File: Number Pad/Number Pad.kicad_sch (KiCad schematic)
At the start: 40 parts

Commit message: Added connectors, labeled keys
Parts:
- added J?: Conn_01x04_Male, symbol Connector:Conn_01x04_Male
- added J?: Conn_01x04_Female, symbol Connector:Conn_01x04_Female
- gave numbers to parts that had none: 18

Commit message: Added footprint libraries
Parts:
- removed J?: Conn_01x04_Male, symbol Connector:Conn_01x04_Male
- removed J?: Conn_01x04_Female, symbol Connector:Conn_01x04_Female
- added J1: Conn_01x05_Female, Connector_JST:JST_PH_S6B-PH-K_1x06_P2.00mm_Horizontal, symbol Connector:Conn_01x05_Female
- added J2: Conn_01x05_Male, Connector_JST:JST_PH_S5B-PH-K_1x05_P2.00mm_Horizontal, symbol Connector:Conn_01x05_Male
- added R1, R2: 100, Resistor_SMD:R_0805_2012Metric, symbol Device:R_Small
- D1, D10, D11, D12, D13, D14, D15, D16, D17, D18, D19, D2, D20, D3, D4, D5, D6, D7, D8, D9: renamed from D?; footprint (none) -> Diode_SMD:D_SOD-123
- renumbered MX_* to MX_*1, MX_+ to MX_+1, MX_- to MX_-1, MX_. to MX_.1, MX_/ to MX_/1, MX_0 to MX_0k1, MX_0 to MX_0k2, MX_Bksp to MX_Bksp1, MX_Enter to MX_Enter1, MX_Enter to MX_Enter2, MX_Num_Lock to MX_Num_Lock1
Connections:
- new net: J2.3 (Pin_3), R2.1
- new net: J1.3 (Pin_3), R1.2
- new net GND: J1.5 (Pin_5), J2.5 (Pin_5)
- new net IN: R2.2
- new net OUT: R1.1
- new net VCC: J1.1 (Pin_1), J2.1 (Pin_1)

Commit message: Assigned footprints
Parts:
- MX_*1, MX_+1, MX_-1, MX_.1, MX_/1, MX_0k1, MX_0k2, MX_1, MX_2, MX_3, MX_4, MX_5, MX_6, MX_7, MX_8, MX_9, MX_Bksp1, MX_Enter1, MX_Enter2, MX_Num_Lock1: footprint (none) -> MX_Alps_Hybrid:MX-1U-NoLED
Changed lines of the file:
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@@
       (effects (font (size 0.508 0.508)))
     )
-    (property "Footprint" "" (id 2) (at 104.775 116.205 0)
+    (property "Footprint" "MX_Alps_Hybrid:MX-1U-NoLED" (id 2) (at 104.775 116.205 0)
       (effects (font (size 1.524 1.524)) hide)
     )
@@
       (effects (font (size 0.508 0.508)))
     )
-    (property "Footprint" "" (id 2) (at 90.805 133.985 0)
+    (property "Footprint" "MX_Alps_Hybrid:MX-1U-NoLED" (id 2) (at 90.805 133.985 0)
       (effects (font (size 1.524 1.524)) hide)
     )
@@
       (effects (font (size 0.508 0.508)))
     )
-    (property "Footprint" "" (id 2) (at 104.775 80.645 0)
+    (property "Footprint" "MX_Alps_Hybrid:MX-1U-NoLED" (id 2) (at 104.775 80.645 0)
       (effects (font (size 1.524 1.524)) hide)
     )
@@
       (effects (font (size 0.508 0.508)))
     )
-    (property "Footprint" "" (id 2) (at 104.775 98.425 0)
+    (property "Footprint" "MX_Alps_Hybrid:MX-1U-NoLED" (id 2) (at 104.775 98.425 0)
       (effects (font (size 1.524 1.524)) hide)
     )
@@
       (effects (font (size 0.508 0.508)))
     )
-    (property "Footprint" "" (id 2) (at 120.015 133.985 0)
+    (property "Footprint" "MX_Alps_Hybrid:MX-1U-NoLED" (id 2) (at 120.015 133.985 0)
       (effects (font (size 1.524 1.524)) hide)
     )
@@
       (effects (font (size 0.508 0.508)))
     )
-    (property "Footprint" "" (id 2) (at 90.805 116.205 0)
+    (property "Footprint" "MX_Alps_Hybrid:MX-1U-NoLED" (id 2) (at 90.805 116.205 0)
       (effects (font (size 1.524 1.524)) hide)
     )
@@
       (effects (font (size 0.508 0.508)))
     )
-    (property "Footprint" "" (id 2) (at 76.835 116.205 0)
+    (property "Footprint" "MX_Alps_Hybrid:MX-1U-NoLED" (id 2) (at 76.835 116.205 0)
       (effects (font (size 1.524 1.524)) hide)
     )
@@
       (effects (font (size 0.508 0.508)))
     )
-    (property "Footprint" "" (id 2) (at 76.835 133.985 0)
+    (property "Footprint" "MX_Alps_Hybrid:MX-1U-NoLED" (id 2) (at 76.835 133.985 0)
       (effects (font (size 1.524 1.524)) hide)
     )
@@
       (effects (font (size 0.508 0.508)))
     )
-    (property "Footprint" "" (id 2) (at 76.835 62.865 0)
+    (property "Footprint" "MX_Alps_Hybrid:MX-1U-NoLED" (id 2) (at 76.835 62.865 0)
       (effects (font (size 1.524 1.524)) hide)
     )
@@
       (effects (font (size 0.508 0.508)))
     )
-    (property "Footprint" "" (id 2) (at 120.015 80.645 0)
+    (property "Footprint" "MX_Alps_Hybrid:MX-1U-NoLED" (id 2) (at 120.015 80.645 0)
       (effects (font (size 1.524 1.524)) hide)
     )
@@
       (effects (font (size 0.508 0.508)))
     )
-    (property "Footprint" "" (id 2) (at 120.015 116.205 0)
+    (property "Footprint" "MX_Alps_Hybrid:MX-1U-NoLED" (id 2) (at 120.015 116.205 0)
       (effects (font (size 1.524 1.524)) hide)
     )
@@
       (effects (font (size 0.508 0.508)))
     )
-    (property "Footprint" "" (id 2) (at 120.015 98.425 0)
+    (property "Footprint" "MX_Alps_Hybrid:MX-1U-NoLED" (id 2) (at 120.015 98.425 0)
       (effects (font (size 1.524 1.524)) hide)
     )
@@
       (effects (font (size 0.508 0.508)))
     )
-    (property "Footprint" "" (id 2) (at 104.775 133.985 0)
+    (property "Footprint" "MX_Alps_Hybrid:MX-1U-NoLED" (id 2) (at 104.775 133.985 0)
       (effects (font (size 1.524 1.524)) hide)
     )
@@
       (effects (font (size 0.508 0.508)))
     )
-    (property "Footprint" "" (id 2) (at 90.805 62.865 0)
+    (property "Footprint" "MX_Alps_Hybrid:MX-1U-NoLED" (id 2) (at 90.805 62.865 0)
       (effects (font (size 1.524 1.524)) hide)
     )
@@
       (effects (font (size 0.508 0.508)))
     )
-    (property "Footprint" "" (id 2) (at 90.805 80.645 0)
+    (property "Footprint" "MX_Alps_Hybrid:MX-1U-NoLED" (id 2) (at 90.805 80.645 0)
       (effects (font (size 1.524 1.524)) hide)
     )
@@
       (effects (font (size 0.508 0.508)))
     )
-    (property "Footprint" "" (id 2) (at 76.835 98.425 0)
+    (property "Footprint" "MX_Alps_Hybrid:MX-1U-NoLED" (id 2) (at 76.835 98.425 0)
       (effects (font (size 1.524 1.524)) hide)
     )
@@
       (effects (font (size 0.508 0.508)))
     )
-    (property "Footprint" "" (id 2) (at 76.835 80.645 0)
+    (property "Footprint" "MX_Alps_Hybrid:MX-1U-NoLED" (id 2) (at 76.835 80.645 0)
       (effects (font (size 1.524 1.524)) hide)
     )
@@
       (effects (font (size 0.508 0.508)))
     )
-    (property "Footprint" "" (id 2) (at 104.775 62.865 0)
+    (property "Footprint" "MX_Alps_Hybrid:MX-1U-NoLED" (id 2) (at 104.775 62.865 0)
       (effects (font (size 1.524 1.524)) hide)
     )
@@
       (effects (font (size 0.508 0.508)))
     )
-    (property "Footprint" "" (id 2) (at 120.015 62.865 0)
+    (property "Footprint" "MX_Alps_Hybrid:MX-1U-NoLED" (id 2) (at 120.015 62.865 0)
       (effects (font (size 1.524 1.524)) hide)
     )
@@
       (effects (font (size 0.508 0.508)))
     )
-    (property "Footprint" "" (id 2) (at 90.805 98.425 0)
+    (property "Footprint" "MX_Alps_Hybrid:MX-1U-NoLED" (id 2) (at 90.805 98.425 0)
       (effects (font (size 1.524 1.524)) hide)
     )
@@
     )
     (path "/d857c13c-d56e-45bf-ad46-b397ec2e0ae0"
-      (reference "MX_*1") (unit 1) (value "MX-NoLED") (footprint "")
+      (reference "MX_*1") (unit 1) (value "MX-NoLED") (footprint "MX_Alps_Hybrid:MX-1U-NoLED")
     )
     (path "/94221e5a-4502-4706-b587-2c1f6ebc7081"
-      (reference "MX_+1") (unit 1) (value "MX-NoLED") (footprint "")
+      (reference "MX_+1") (unit 1) (value "MX-NoLED") (footprint "MX_Alps_Hybrid:MX-1U-NoLED")
     )
     (path "/e034d7d8-b6b0-48dd-a2fb-3ef9e5485732"
-      (reference "MX_-1") (unit 1) (value "MX-NoLED") (footprint "")
+      (reference "MX_-1") (unit 1) (value "MX-NoLED") (footprint "MX_Alps_Hybrid:MX-1U-NoLED")
     )
     (path "/bc31409d-138d-45b6-ab33-c15c4b90a8c1"
-      (reference "MX_.1") (unit 1) (value "MX-NoLED") (footprint "")
+      (reference "MX_.1") (unit 1) (value "MX-NoLED") (footprint "MX_Alps_Hybrid:MX-1U-NoLED")
     )
     (path "/c2f733ad-ae8f-48a6-bc32-ea854aee0561"
-      (reference "MX_/1") (unit 1) (value "MX-NoLED") (footprint "")
+      (reference "MX_/1") (unit 1) (value "MX-NoLED") (footprint "MX_Alps_Hybrid:MX-1U-NoLED")
     )
     (path "/8e805ade-fa03-4a15-81b0-f7f34d179d14"
-      (reference "MX_0k1") (unit 1) (value "MX-NoLED") (footprint "")
+      (reference "MX_0k1") (unit 1) (value "MX-NoLED") (footprint "MX_Alps_Hybrid:MX-1U-NoLED")
     )
     (path "/32bf3049-4aa9-4c86-abb1-715dfc213dc2"
-      (reference "MX_0k2") (unit 1) (value "MX-NoLED") (footprint "")
+      (reference "MX_0k2") (unit 1) (value "MX-NoLED") (footprint "MX_Alps_Hybrid:MX-1U-NoLED")
     )
     (path "/81ebf916-3913-4b41-b59e-256ce94edddb"
-      (reference "MX_1") (unit 1) (value "MX-NoLED") (footprint "")
+      (reference "MX_1") (unit 1) (value "MX-NoLED") (footprint "MX_Alps_Hybrid:MX-1U-NoLED")
     )
     (path "/674df612-450c-4fcc-aad3-5c7e9c376f43"
-      (reference "MX_2") (unit 1) (value "MX-NoLED") (footprint "")
+      (reference "MX_2") (unit 1) (value "MX-NoLED") (footprint "MX_Alps_Hybrid:MX-1U-NoLED")
     )
     (path "/1b7828d9-18a8-4156-a5d5-0487faba3c23"
-      (reference "MX_3") (unit 1) (value "MX-NoLED") (footprint "")
+      (reference "MX_3") (unit 1) (value "MX-NoLED") (footprint "MX_Alps_Hybrid:MX-1U-NoLED")
     )
     (path "/d723d9b0-8011-4297-83f4-fe6ebfa77c62"
-      (reference "MX_4") (unit 1) (value "MX-NoLED") (footprint "")
+      (reference "MX_4") (unit 1) (value "MX-NoLED") (footprint "MX_Alps_Hybrid:MX-1U-NoLED")
     )
     (path "/fdac5475-80bd-472e-a630-30515f47938b"
-      (reference "MX_5") (unit 1) (value "MX-NoLED") (footprint "")
+      (reference "MX_5") (unit 1) (value "MX-NoLED") (footprint "MX_Alps_Hybrid:MX-1U-NoLED")
     )
     (path "/46442973-57c2-4198-8d8f-df43e9495361"
-      (reference "MX_6") (unit 1) (value "MX-NoLED") (footprint "")
+      (reference "MX_6") (unit 1) (value "MX-NoLED") (footprint "MX_Alps_Hybrid:MX-1U-NoLED")
     )
     (path "/d79bea14-7996-4d77-9ba6-af3dd6991c01"
-      (reference "MX_7") (unit 1) (value "MX-NoLED") (footprint "")
+      (reference "MX_7") (unit 1) (value "MX-NoLED") (footprint "MX_Alps_Hybrid:MX-1U-NoLED")
     )
     (path "/c8d099c1-e32a-4864-9de8-91f33723217f"
-      (reference "MX_8") (unit 1) (value "MX-NoLED") (footprint "")
+      (reference "MX_8") (unit 1) (value "MX-NoLED") (footprint "MX_Alps_Hybrid:MX-1U-NoLED")
     )
     (path "/4472a952-639b-456f-b54f-9620fac1383c"
-      (reference "MX_9") (unit 1) (value "MX-NoLED") (footprint "")
+      (reference "MX_9") (unit 1) (value "MX-NoLED") (footprint "MX_Alps_Hybrid:MX-1U-NoLED")
     )
     (path "/b4c3319e-03db-429f-8b87-f076f418c3ee"
-      (reference "MX_Bksp1") (unit 1) (value "MX-NoLED") (footprint "")
+      (reference "MX_Bksp1") (unit 1) (value "MX-NoLED") (footprint "MX_Alps_Hybrid:MX-1U-NoLED")
     )
     (path "/a6ebafa7-e171-4f30-beb9-a0b9d632d00b"
-      (reference "MX_Enter1") (unit 1) (value "MX-NoLED") (footprint "")
+      (reference "MX_Enter1") (unit 1) (value "MX-NoLED") (footprint "MX_Alps_Hybrid:MX-1U-NoLED")
     )
     (path "/4cdf5ed0-32f4-4457-a171-ffaa54f6f148"
-      (reference "MX_Enter2") (unit 1) (value "MX-NoLED") (footprint "")
+      (reference "MX_Enter2") (unit 1) (value "MX-NoLED") (footprint "MX_Alps_Hybrid:MX-1U-NoLED")
     )
     (path "/91209565-0b3a-430f-88cf-4fc8f35ad67e"
-      (reference "MX_Num_Lock1") (unit 1) (value "MX-NoLED") (footprint "")
+      (reference "MX_Num_Lock1") (unit 1) (value "MX-NoLED") (footprint "MX_Alps_Hybrid:MX-1U-NoLED")
     )
     (path "/8a328004-e44b-418e-b23f-311b446f7fc7"

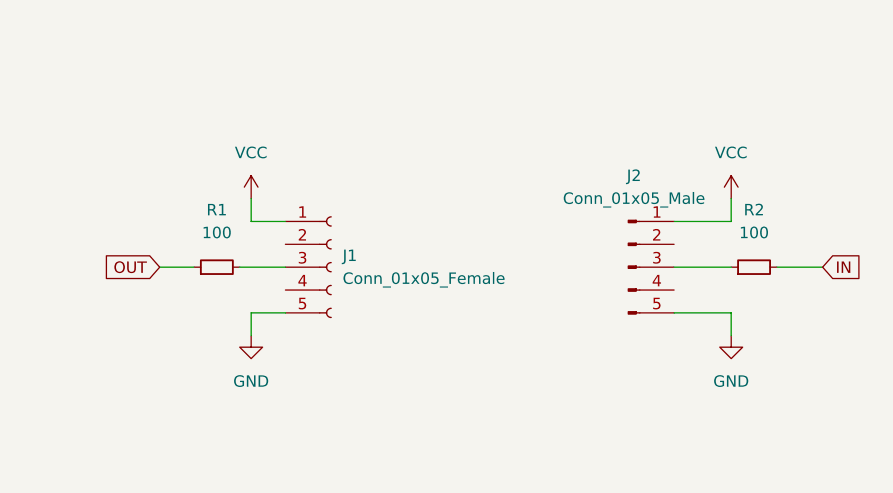
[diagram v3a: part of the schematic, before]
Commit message: Edited connectors a tad
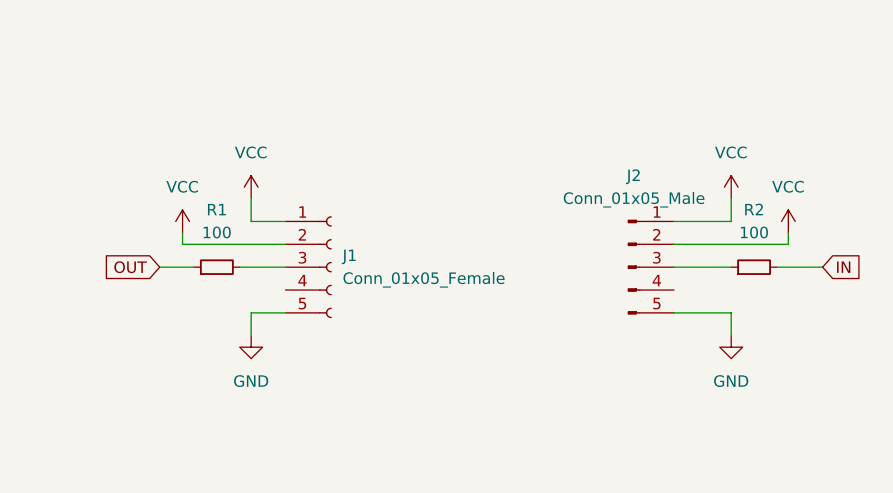
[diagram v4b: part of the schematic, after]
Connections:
- net VCC: now also J1.2 (Pin_2), J2.2 (Pin_2)
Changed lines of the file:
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@@
+    (stroke (width 0) (type default) (color 0 0 0 0))
+  )
+  (wire (pts (xy 184.15 64.77) (xy 184.15 63.5))
     (stroke (width 0) (type default) (color 0 0 0 0))
   )
@@
     (stroke (width 0) (type default) (color 0 0 0 0))
   )
+  (wire (pts (xy 238.76 64.77) (xy 251.46 64.77))
+    (stroke (width 0) (type default) (color 0 0 0 0))
+  )
   (wire (pts (xy 129.54 67.31) (xy 134.62 67.31))
     (stroke (width 0) (type default) (color 0 0 0 0))
@@
     (stroke (width 0) (type default) (color 0 0 0 0))
   )
+  (wire (pts (xy 195.58 64.77) (xy 184.15 64.77))
+    (stroke (width 0) (type default) (color 0 0 0 0))
+  )
   (wire (pts (xy 114.3 85.09) (xy 119.38 85.09))
     (stroke (width 0) (type default) (color 0 0 0 0))
@@
   )
   (wire (pts (xy 77.47 107.95) (xy 86.36 107.95))
+    (stroke (width 0) (type default) (color 0 0 0 0))
+  )
+  (wire (pts (xy 251.46 64.77) (xy 251.46 63.5))
     (stroke (width 0) (type default) (color 0 0 0 0))
   )
@@
     (pin "2")
   )
+  (symbol (lib_id "power:VCC") (at 184.15 63.5 0) (unit 1)
+    (in_bom yes) (on_board yes) (fields_autoplaced)
+    (property "Reference" "#PWR?" (id 0) (at 184.15 67.31 0)
+      (effects (font (size 1.27 1.27)) hide)
+    )
+    (property "Value" "VCC" (id 1) (at 184.15 58.42 0))
+    (property "Footprint" "" (id 2) (at 184.15 63.5 0)
+      (effects (font (size 1.27 1.27)) hide)
+    )
+    (property "Datasheet" "" (id 3) (at 184.15 63.5 0)
+      (effects (font (size 1.27 1.27)) hide)
+    )
+    (pin "1")
+  )
   (symbol (lib_id "MX_Alps_Hybrid:MX-NoLED") (at 106.68 80.01 0) (unit 1)
     (in_bom yes) (on_board yes) (fields_autoplaced)
@@
     (pin "1")
     (pin "2")
+  )
+  (symbol (lib_id "power:VCC") (at 251.46 63.5 0) (unit 1)
+    (in_bom yes) (on_board yes) (fields_autoplaced)
+    (property "Reference" "#PWR?" (id 0) (at 251.46 67.31 0)
+      (effects (font (size 1.27 1.27)) hide)
+    )
+    (property "Value" "VCC" (id 1) (at 251.46 58.42 0))
+    (property "Footprint" "" (id 2) (at 251.46 63.5 0)
+      (effects (font (size 1.27 1.27)) hide)
+    )
+    (property "Datasheet" "" (id 3) (at 251.46 63.5 0)
+      (effects (font (size 1.27 1.27)) hide)
+    )
+    (pin "1")
   )
   (symbol (lib_id "MX_Alps_Hybrid:MX-NoLED") (at 135.89 62.23 0) (unit 1)
@@
       (reference "#PWR0104") (unit 1) (value "GND") (footprint "")
     )
+    (path "/c7cb3d1e-d141-4fb0-bf13-e0a177575842"
+      (reference "#PWR?") (unit 1) (value "VCC") (footprint "")
+    )
+    (path "/da7987ef-0854-4d4e-ba0b-bced4e5baee0"
+      (reference "#PWR?") (unit 1) (value "VCC") (footprint "")
+    )
     (path "/a8e848d2-b383-4dd1-aee0-bc9c1387c47b"

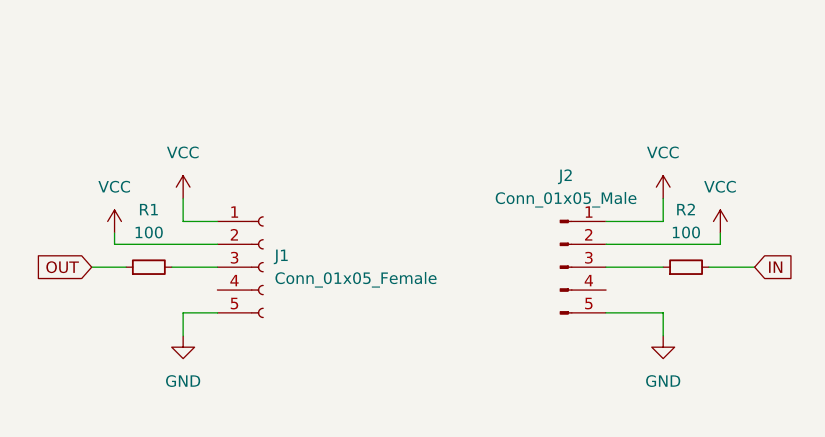
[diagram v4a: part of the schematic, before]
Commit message: Fixed issue with connector
accidentally had two Vcc on each connector
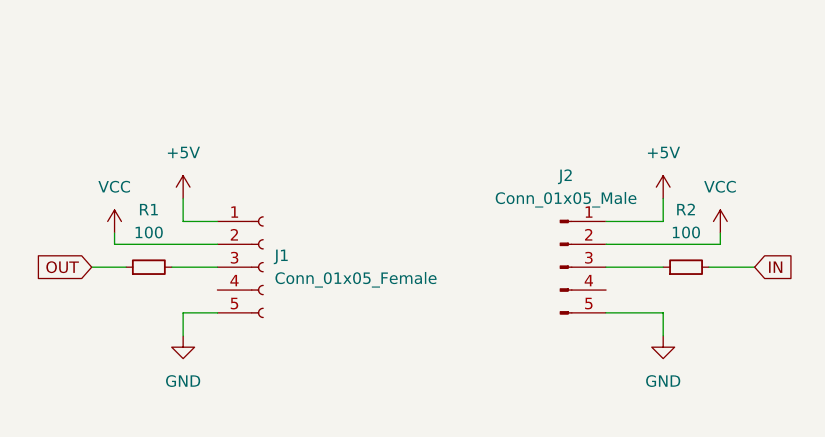
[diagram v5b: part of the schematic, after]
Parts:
- J1: footprint Connector_JST:JST_PH_S6B-PH-K_1x06_P2.00mm_Horizontal -> Connector_JST:JST_PH_S5B-PH-K_1x05_P2.00mm_Horizontal
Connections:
- net VCC: no longer J1.1 (Pin_1), J2.1 (Pin_1)
- new net +5V: J1.1 (Pin_1), J2.1 (Pin_1)
